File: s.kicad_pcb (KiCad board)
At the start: 2 copper layers, 190 x 76 mm, 98 parts, among them J2 UART connector, J4 Conn_01x02_Pin, J5 USB4105-GF-A, SW1 Z, SW10 D, SW11 S, SW12 K, SW13 W, SW14 R, SW15 STAR, SW16 R, SW17 B, SW18 G, SW19 S, SW2 T, SW20 Z, SW21 A, SW22 O, SW23 NUM, SW24 E, SW25 U, SW26 210-4MS, SW27 09.03290.01, SW28 EVP-AA202K, SW3 P, SW4 H, SW5 STAR, SW6 F, SW7 P, SW8 L, SW9 T, U1 ESP32-S3-WROOM-1, U2 MCP1825S, U3 MCP1825S, U4 AP9101CK, U5 MCP73831-2-OT, U6 DMG6968U-7, U7 DMG6968U-7

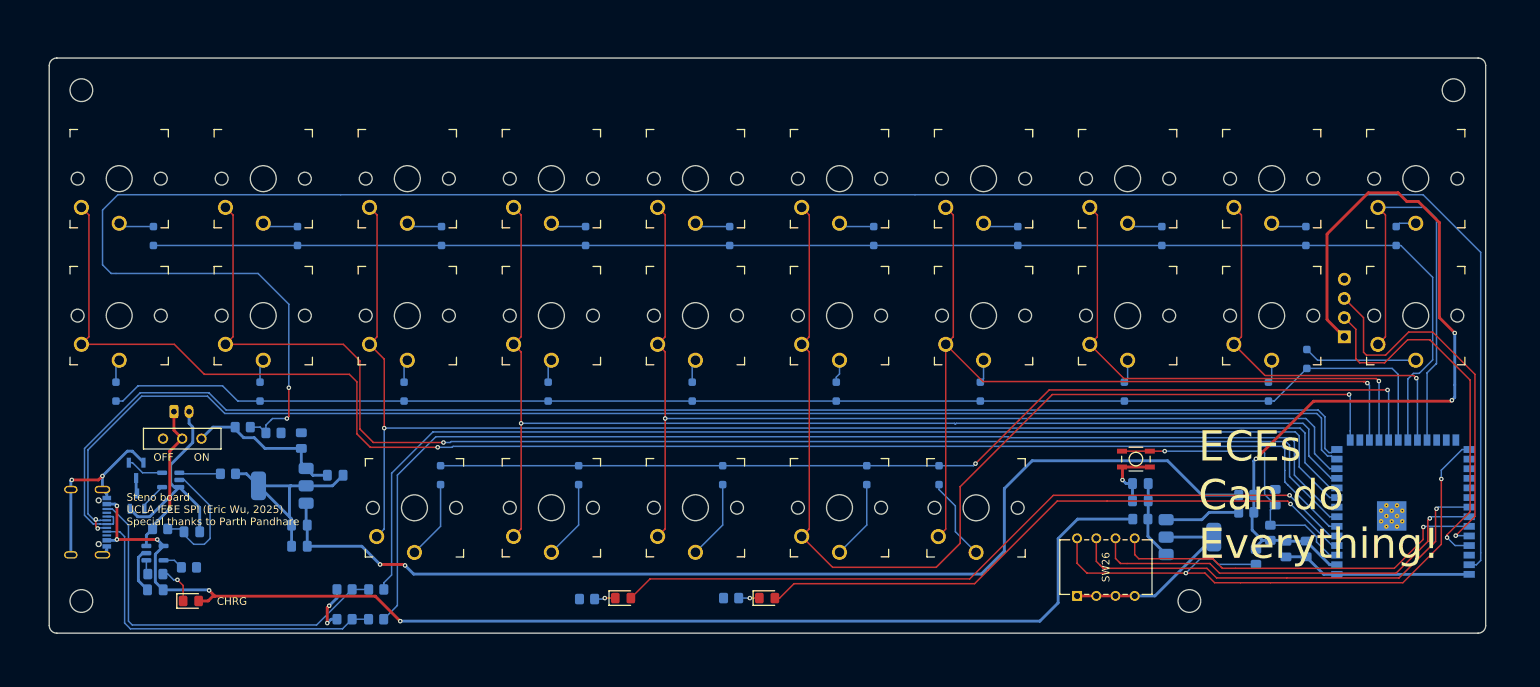
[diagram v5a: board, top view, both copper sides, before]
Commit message: add fill zones for GND
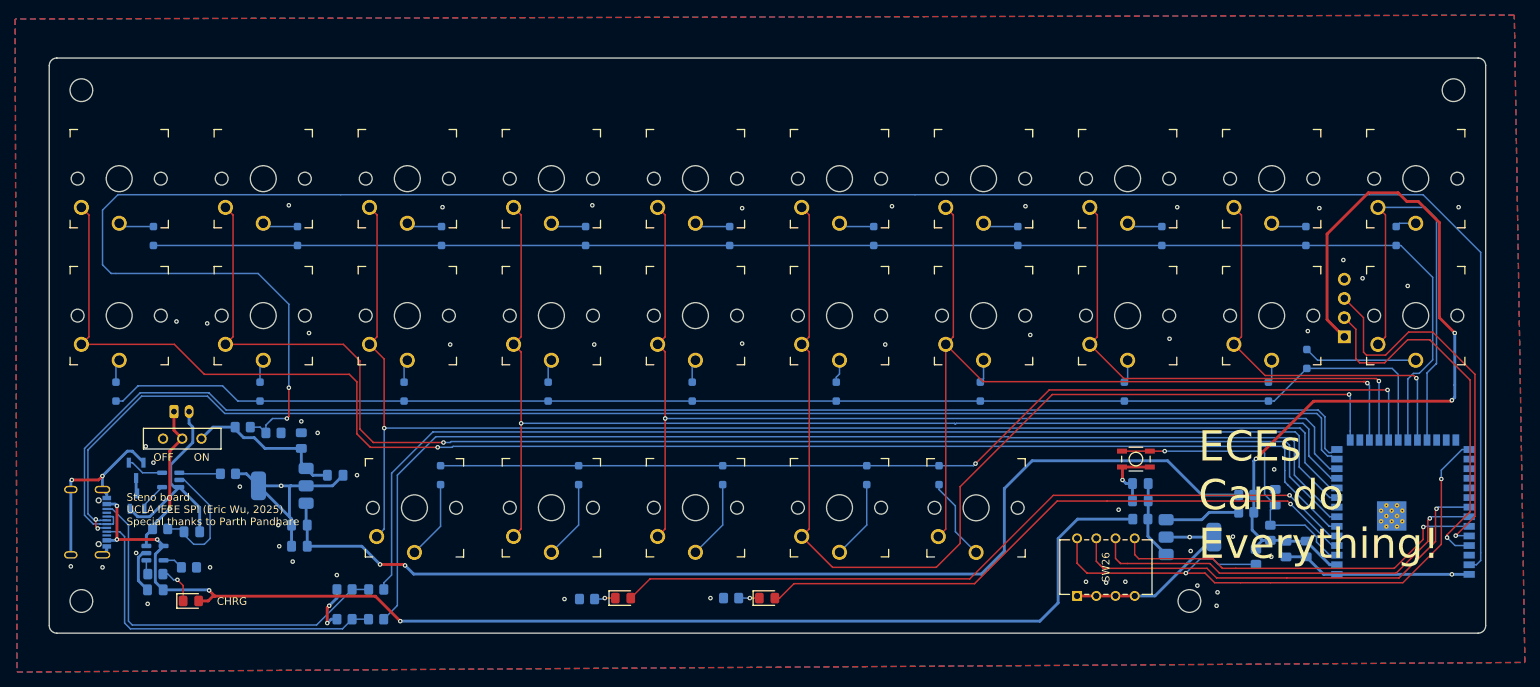
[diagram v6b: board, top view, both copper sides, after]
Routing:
- net GND: vias 5 -> 58
- added copper zone on B.Cu, net GND
- added copper zone on F.Cu, net GND

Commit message: add some vias
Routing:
- net GND: vias 58 -> 67
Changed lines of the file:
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@@
+	)
+	(via
+		(at 145.415 111.252)
+		(size 0.6)
+		(drill 0.3)
+		(layers "F.Cu" "B.Cu")
+		(free yes)
+		(net 1)
 	)
 	(via
@@
 	)
 	(via
+		(at 96.012 99.949)
+		(size 0.6)
+		(drill 0.3)
+		(layers "F.Cu" "B.Cu")
+		(free yes)
+		(net 1)
+	)
+	(via
 		(at 84.836 78.359)
 		(size 0.6)
@@
 	)
 	(via
+		(at 132.08 111.252)
+		(size 0.6)
+		(drill 0.3)
+		(layers "F.Cu" "B.Cu")
+		(free yes)
+		(net 1)
+	)
+	(via
 		(at 85.344 125.476)
 		(size 0.6)
@@
 	)
 	(via
+		(at 108.331 111.506)
+		(size 0.6)
+		(drill 0.3)
+		(layers "F.Cu" "B.Cu")
+		(free yes)
+		(net 1)
+	)
+	(via
 		(at 87.503 95.25)
 		(size 0.6)
@@
 	)
 	(via
+		(at 58.547 99.822)
+		(size 0.6)
+		(drill 0.3)
+		(layers "F.Cu" "B.Cu")
+		(free yes)
+		(net 1)
+	)
+	(via
 		(at 106.172 96.774)
 		(size 0.6)
@@
 	)
 	(via
+		(at 117.983 111.379)
+		(size 0.6)
+		(drill 0.3)
+		(layers "F.Cu" "B.Cu")
+		(free yes)
+		(net 1)
+	)
+	(via
 		(at 204.978 128.651)
 		(size 0.6)
@@
 	)
 	(via
+		(at 66.548 99.568)
+		(size 0.6)
+		(drill 0.3)
+		(layers "F.Cu" "B.Cu")
+		(free yes)
+		(net 1)
+	)
+	(via
 		(at 232.791 89.027)
 		(size 0.6)
@@
 	)
 	(via
+		(at 98.425 111.76)
+		(size 0.6)
+		(drill 0.3)
+		(layers "F.Cu" "B.Cu")
+		(free yes)
+		(net 1)
+	)
+	(via
 		(at 66.167 131.064)
 		(size 0.6)
@@
 		(size 0.6)
 		(drill 0.3)
+		(layers "F.Cu" "B.Cu")
+		(free yes)
+		(net 1)
+	)
+	(via
+		(at 78.105 98.933)
+		(size 0.6)
+		(drill 0.3)
